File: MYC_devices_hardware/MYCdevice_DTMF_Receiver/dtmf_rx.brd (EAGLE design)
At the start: 79.4 x 49.2 mm, 45 parts, among them IC1 MEGA8-P, IC2 MAX232, IC3 7805TV, IC4 CM8870CP, Q1 20MHz, Q2 20MHz, X1 8-15V, X2 1503_09, X3 1503_09, X4 RS232

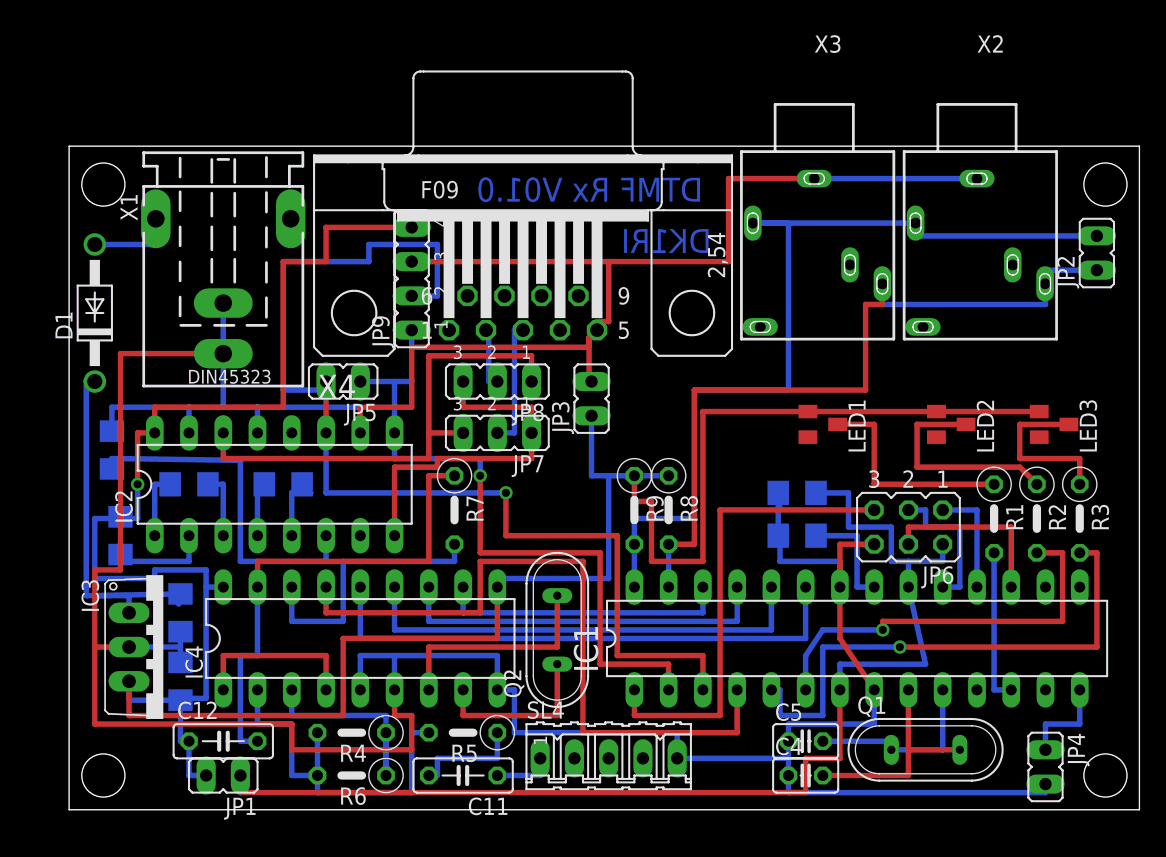
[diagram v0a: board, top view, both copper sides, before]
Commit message: DTMF TRX (MT8880) added
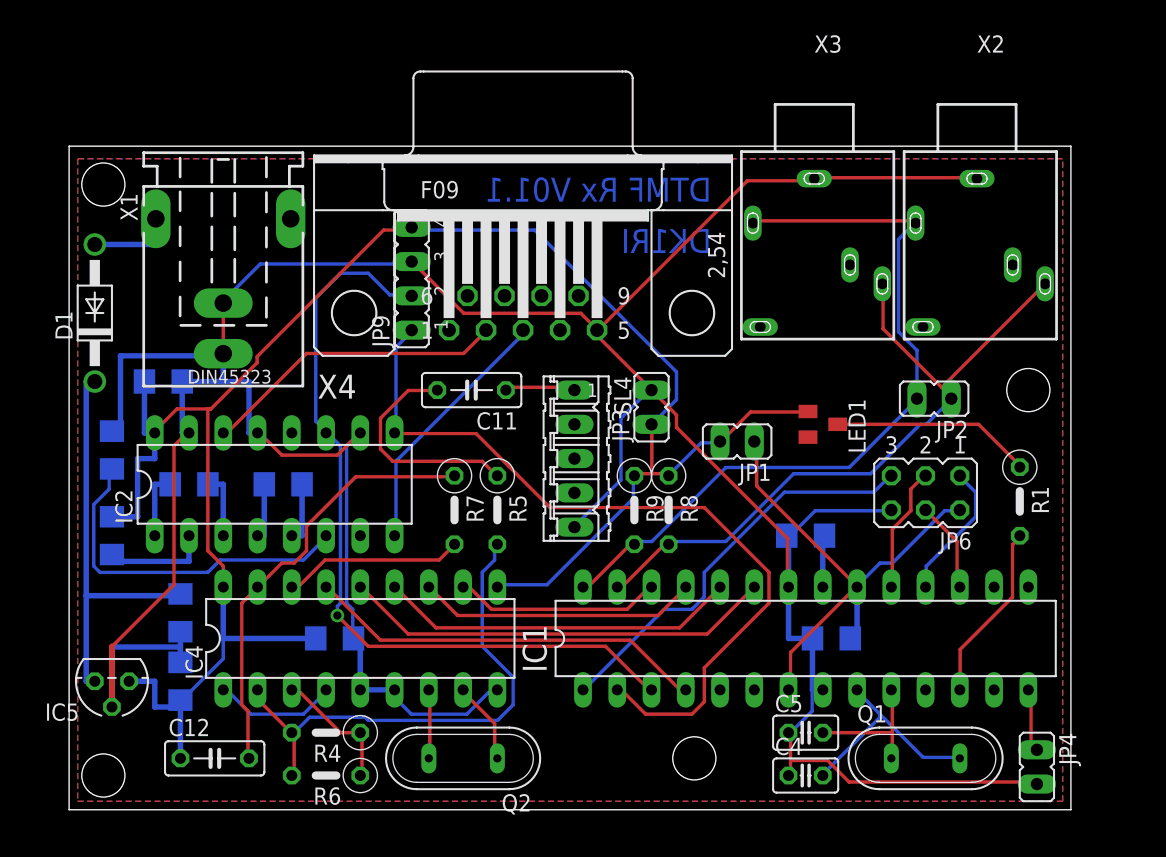
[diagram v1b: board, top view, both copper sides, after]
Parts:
- removed IC3: 7805TV, linear:TO220V
- removed JP5: Rs232-TTL, jumper:JP1
- removed JP7, JP8: DTE/DCE, jumper:JP2
- removed LED2, LED3: PL006-WCY01, led:SOT23
- removed R2, R3: 4k7, resistor:0207/5V
- added C13, C14: 22uF 1210, rcl:C1206
- added IC5: 78L05Z, linear:TO92
- Q2: value 20MHz -> 3,579545MHz
- R5: value 102k -> 10k
- moved JP1 45.4 mm to (49.5, 27.3)
- moved C11 28.6 mm to (29.8, 31.1)
- moved SL4 22.4 mm to (37.5, 26.0), turned to 270 degrees
- moved R5 16.7 mm to (31.8, 22.2), turned to 270 degrees
- moved JP2 16.2 mm to (64.1, 30.5), turned to 90 degrees
- moved Q2 11.8 mm to (29.2, 3.81), turned to 180 degrees
- moved C6 11.1 mm to (56.5, 12.7)
- moved JP3 4.49 mm to (43.2, 29.8)
- moved IC1 3.81 mm to (54.6, 12.7)
- moved JP6 2.84 mm to (63.5, 23.5)
- moved R1 2.29 mm to (70.5, 22.9)
- moved R4 1.90 mm to (19.1, 5.71)
- moved R6 1.90 mm to (19.1, 2.54)
- moved C12 1.42 mm to (10.8, 3.81)
- moved JP4 0.64 mm to (71.8, 3.17)
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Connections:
- removed net N$10: IC2.14, JP7.3, JP8.1
- removed net N$23: IC1.6, R2.2
- removed net N$48: LED3.3, R3.1
- removed net N$49: LED2.3, R2.1
- removed net N$51: IC1.5, R3.2
- removed net N$9: JP7.2, X4.3
- net GND: now also C13.2, C14.2, IC5.2; no longer IC3.2
- net N$11: now also X4.3; no longer JP7.1, JP8.3
- net N$12: no longer JP5.2
- net N$2: no longer JP5.1
- net N$33: now also IC5.3; no longer IC3.1
- net N$4: now also IC2.14; no longer JP8.2
- net VDD: now also C13.1, C14.1, IC5.1; no longer IC3.3, LED2.1, LED3.1
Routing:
- net VDD: track 197.6 -> 142.6 mm, vias 1 -> 0
- net N$44: track 85.1 -> 38.1 mm
- net N$51: track 39.4 -> 0.00 mm, vias 1 -> 0
- net GND: track 297.4 -> 260.5 mm
- net N$10: track 36.8 -> 0.00 mm
- net N$23: track 30.2 -> 0.00 mm, vias 1 -> 0
- net N$12: track 82.5 -> 58.6 mm
- net N$42: track 52.1 -> 29.8 mm
- net N$4: track 4.65 -> 22.8 mm
- net N$49: track 16.2 -> 0.00 mm
- net N$48: track 12.5 -> 0.00 mm
- net N$31: track 16.5 -> 5.13 mm
- net N$25: track 27.9 -> 38.5 mm
- net N$22: track 67.5 -> 57.3 mm
- net N$9: track 9.53 -> 0.00 mm
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- added copper zone on layer 1, net GND
- added copper zone on layer 16, net GND
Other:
- board size 79.4 x 49.2 mm -> 74.3 x 49.2 mm
- board text added: "DTMF Rx V01.1"
- board text removed: "DTMF Rx V01.0"

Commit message: new board, bacom with includes
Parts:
- removed SL4: DTMF/RC5, con-amp-quick:05P
- removed X2, X3: 1503_09, con-lumberg:1503_09
- added IC3: PCA9517, PCA9517:SO-08
- added JP5: Reset, jumper:JP1
- added JP8: 5V, jumper:JP1
- added R10: 10k, resistor:R1206
- added R11: 4k7, resistor:R1206
- added R2, R3: * see manual, resistor:R1206
- added SL1, SL2: I2C, con-amp-quick:03P
- added SL3: DTMF, con-amp-quick:03P
- C1, C13, C14, C2, C3, C6: value 22uF 1210 -> 22uF
- C10, C7, C8, C9: value 22u 1210 -> 22uF
- IC4: value CM8870CP -> 78L05Z; device california-micro-devices:DIL18 -> linear:TO92
- IC5: value 78L05Z -> CM8870CP; device linear:TO92 -> california-micro-devices:DIL18
- JP2: value I2C -> 3V/5V; device jumper:JP1 -> jumper:JP2
- JP3: value 5V -> SDA
- JP4: value Reset -> SCL
- R1: value 4k7 -> * see manual; device resistor:0207/5V -> resistor:R1206
- R4: value - -> * see manual; device resistor:0207/5V -> resistor:R1206
- R5: value 10k -> 1k; device resistor:0207/5V -> resistor:R1206
- R6: value 71,5k -> 1k5; device resistor:0207/5V -> resistor:R1206
- R7: device resistor:0207/5V -> resistor:R1206
- R8: value 4k7 -> 71,5k; device resistor:0207/5V -> resistor:R1206
- R9: value 4k7 -> -; device resistor:0207/5V -> resistor:R1206
- moved JP2 54.8 mm to (9.53, 26.0), turned to 0 degrees
- moved C10 47.2 mm to (48.3, 12.7), turned to 180 degrees
- moved C14 38.5 mm to (45.1, 26.0)
- moved R4 37.9 mm to (51.4, 25.4), flipped to the bottom, turned to 0 degrees
- moved R9 37.5 mm to (8.26, 5.71), flipped to the bottom, turned to 0 degrees
- moved R8 33.6 mm to (15.2, 5.71), flipped to the bottom, turned to 0 degrees
- moved LED1 32.0 mm to (34.9, 4.45)
- moved JP4 31.6 mm to (63.5, 33.7)
- moved R6 30.4 mm to (5.71, 29.8), flipped to the bottom, turned to 0 degrees
- moved C7 29.3 mm to (38.1, 26.0)
- moved C6 27.6 mm to (32.4, 26.0), turned to 180 degrees
- moved IC2 22.9 mm to (38.1, 26.0)
- moved C9 22.4 mm to (25.4, 22.9), turned to 270 degrees
- moved R5 19.9 mm to (13.3, 29.8), flipped to the bottom, turned to 180 degrees
- moved R7 18.5 mm to (12.7, 12.7), flipped to the bottom, turned to 180 degrees
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- renumbered JP9 to JP7
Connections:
- removed net N$22: IC1.28, JP2.2, R9.2, X2.2, X3.2
- new net N$10: JP2.1, R5.1, R6.2
- new net N$23: IC1.28, IC3.7, JP4.2, R4.2
- new net N$36: IC1.27, IC3.6, JP3.2, R3.2
- new net N$39: IC3.2, JP4.1, R2.1, SL1.2, SL2.2
- new net N$43: IC3.1, JP2.2, R1.2, R2.2
- net C13: now also C6.1; no longer C7.1
- net GND: now also C10.2, C9.1, IC3.4, IC4.2, IC5.5, IC5.6, IC5.9, JP5.2, JP8.2, R6.1, SL1.1, SL2.1, SL3.1; no longer C10.1, C6.2, IC4.5, IC4.6, IC4.9, IC5.2, JP3.2, JP4.2, SL4.5, X2.1, X3.1
- net N$1: now also R11.2; no longer R1.2
- net N$13: now also C7.1; no longer C8.1
- net N$14: now also C6.2; no longer C7.2
- net N$16: now also C8.1; no longer C9.1
- net N$17: now also C9.2; no longer C10.2
- net N$21: now also SL3.3; no longer SL4.1
- net N$24: now also R10.1; no longer R5.1
- net N$25: now also IC5.2, R10.2, R8.2, R9.2; no longer IC4.2, R4.2, R5.2, R6.2
- net N$26: now also IC5.3, R8.1, R9.1; no longer IC4.3, R4.1, R6.1
- net N$29: now also IC5.8; no longer IC4.8
- net N$3: now also C7.2; no longer C8.2
- net N$30: now also IC5.13; no longer IC4.13
- net N$31: now also IC5.7; no longer IC4.7
- net N$32: now also IC5.16; no longer IC4.16
- net N$33: now also IC4.3; no longer IC5.3
- net N$34: now also IC5.11; no longer IC4.11
- net N$38: now also IC5.12; no longer IC4.12
- net N$40: now also IC5.17; no longer IC4.17
- net N$42: now also IC5.15; no longer IC4.15
- net N$44: now also C10.1; no longer C6.1
- net N$5: now also IC3.3, JP3.1, R1.1, SL1.3, SL2.3; no longer IC1.27, JP2.1, R8.2, X2.3, X3.3
- net N$50: now also R11.1; no longer R1.1
- net N$6: now also JP5.1; no longer JP4.1
- net N$7: now also IC5.1, IC5.4; no longer IC4.1, IC4.4
- net N$8: now also IC5.14; no longer IC4.14
- net VDD: now also C8.2, IC3.5, IC3.8, IC4.1, IC5.10, IC5.18, JP2.3, JP8.1, R3.1, R4.1, R5.2; no longer C9.2, IC4.10, IC4.18, IC5.1, JP3.1, R8.1, R9.1
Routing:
- net N$23: track 0.00 -> 104.9 mm
- net N$43: track 0.00 -> 104.0 mm, vias 0 -> 1
- net VDD: track 142.6 -> 240.4 mm, vias 0 -> 1
- net N$22: track 57.3 -> 0.00 mm
- net N$36: track 0.00 -> 38.5 mm
- net N$39: track 0.00 -> 28.9 mm
- net N$5: track 52.3 -> 24.1 mm
- net N$25: track 38.5 -> 15.8 mm
- net GND: track 260.5 -> 238.6 mm
- net N$24: track 16.8 -> 32.8 mm
- net N$4: track 22.8 -> 7.13 mm
- net N$6: track 4.74 -> 17.9 mm
- net N$33: track 30.6 -> 17.8 mm
- net N$10: track 0.00 -> 11.5 mm
- net N$50: track 14.9 -> 5.84 mm, vias 0 -> 1
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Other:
- board size 74.3 x 49.2 mm -> 67.9 x 49.2 mm
- board text added: "1"
- board text added: "3"
- board text added: "5"
- board text added: "DTMFRX V04.1"
- board text removed: "DTMF Rx V01.1"
